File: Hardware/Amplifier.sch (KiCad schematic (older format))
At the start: 1 part, among them U401 PAM8019KGR

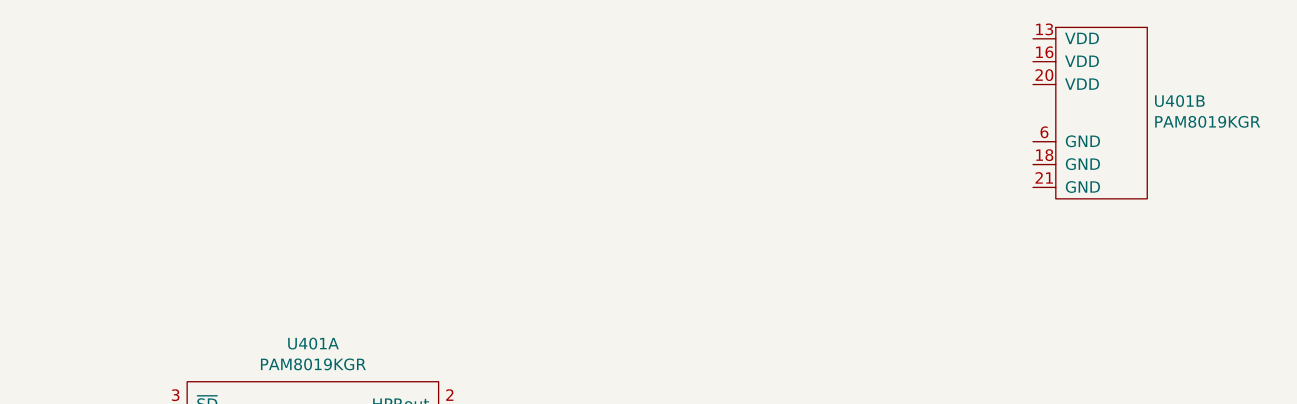
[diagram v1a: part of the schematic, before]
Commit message: Now putting in power and passives.
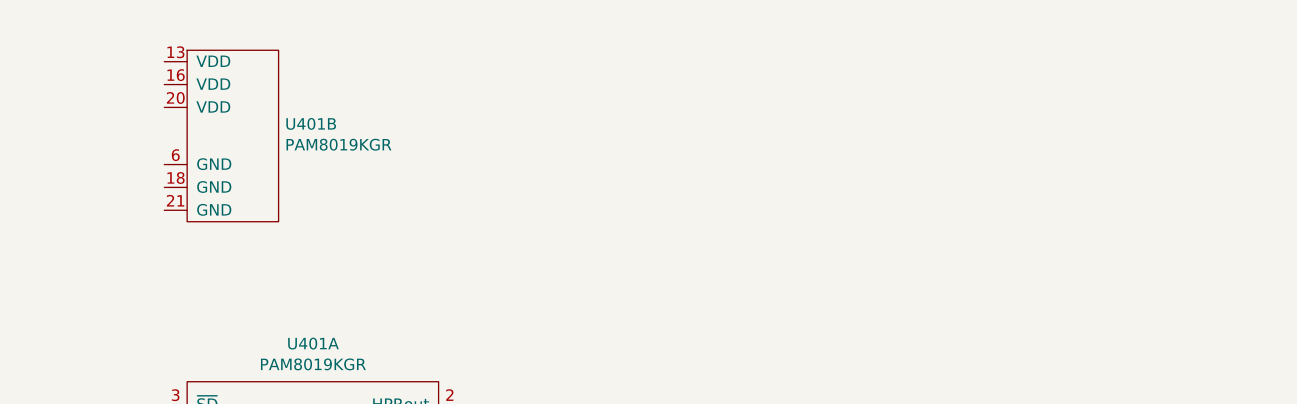
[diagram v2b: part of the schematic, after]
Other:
- moved on the sheet: U401B
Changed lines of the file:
@@
 L OHMC2022:PAM8019KGR U401
 U 2 1 61361640
-P 8850 1800
+P 5050 1900
 AR Path="/611E3218/611E330D/61361640" Ref="U401"  Part="2"
 AR Path="/61375092/611E330D/61361640" Ref="U?"  Part="2"
-F 0 "U401" H 9078 1826 50  0000 L CNN
-F 1 "PAM8019KGR" H 9078 1735 50  0000 L CNN
-F 2 "Package_DFN_QFN:QFN-20-1EP_4x4mm_P0.5mm_EP2.6x2.6mm" H 8550 800 50  0001 C CNN
-F 3 "www.diodes.com/assets/Datasheets/PAM8019.pdf" H 8550 800 50  0001 C CNN
-	2    8850 1800
+F 0 "U401" H 5278 1926 50  0000 L CNN
+F 1 "PAM8019KGR" H 5278 1835 50  0000 L CNN
+F 2 "Package_DFN_QFN:QFN-20-1EP_4x4mm_P0.5mm_EP2.6x2.6mm" H 4750 900 50  0001 C CNN
+F 3 "www.diodes.com/assets/Datasheets/PAM8019.pdf" H 4750 900 50  0001 C CNN
+	2    5050 1900
 	1    0    0    -1
 $EndComp

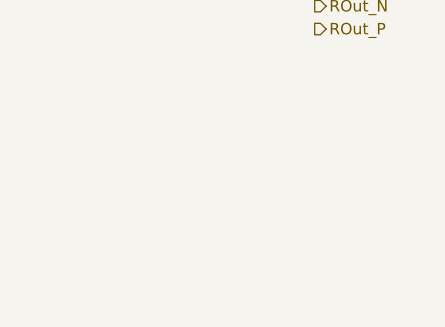
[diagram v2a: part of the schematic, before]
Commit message: Power connectivity going in.
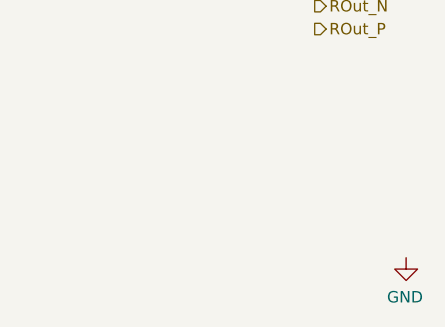
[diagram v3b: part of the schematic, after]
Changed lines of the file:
@@
 Text HLabel 7550 3600 2    50   Output ~ 0
 ROut_P
+$Comp
+L power:GND #PWR?
+U 1 1 613B2112
+P 7950 4600
+F 0 "#PWR?" H 7950 4350 50  0001 C CNN
+F 1 "GND" H 7955 4427 50  0000 C CNN
+F 2 "" H 7950 4600 50  0001 C CNN
+F 3 "" H 7950 4600 50  0001 C CNN
+	1    7950 4600
+	-1   0    0    -1
+$EndComp
 $EndSCHEMATC

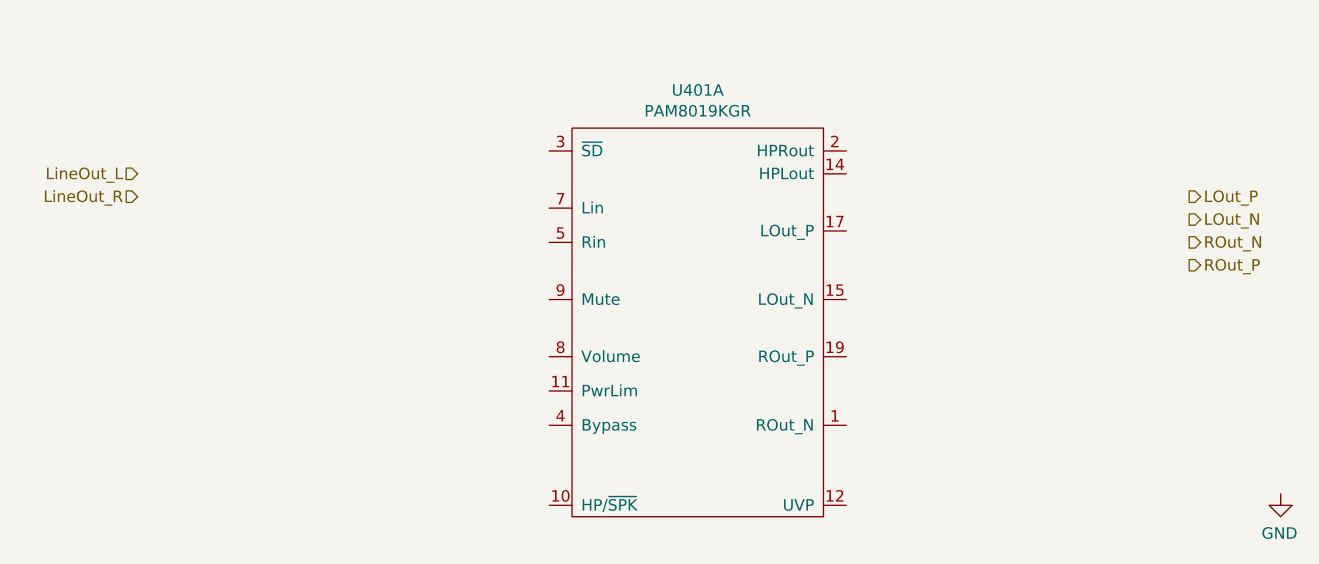
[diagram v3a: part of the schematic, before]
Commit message: Putting in some connectivity. More passives.
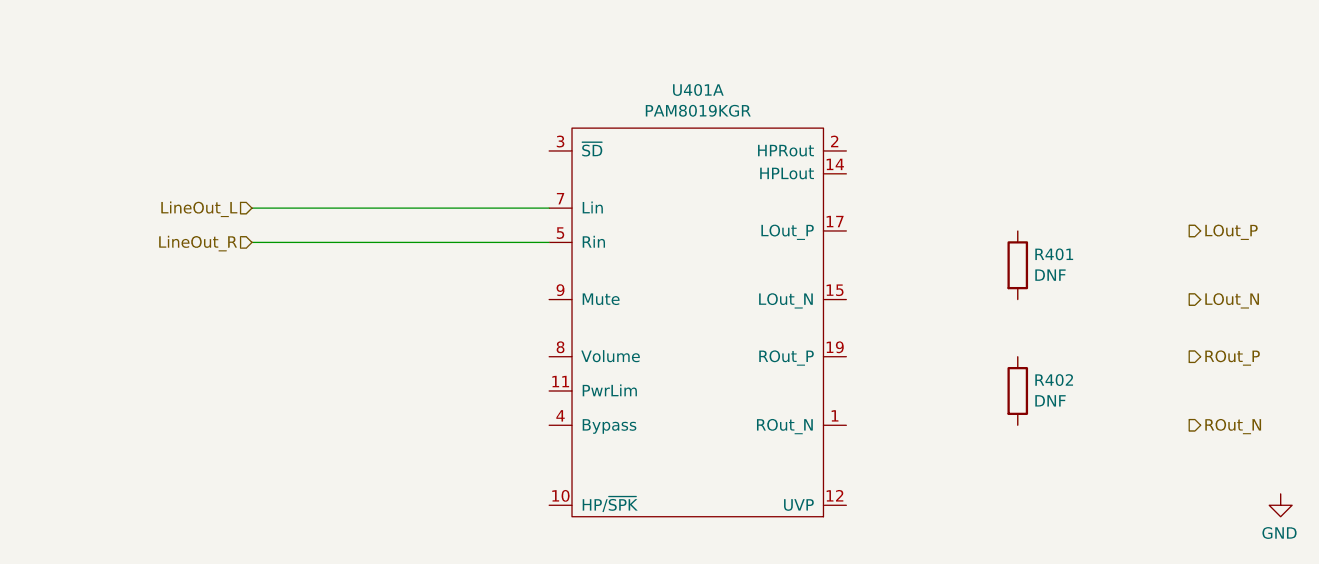
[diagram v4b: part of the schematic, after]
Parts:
- added R401, R402: DNF, Resistor_SMD:R_0603_1608Metric, symbol Device:R
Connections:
- net LineOut_L: now also U401.7 (Lin)
- net LineOut_R: now also U401.5 (Rin)
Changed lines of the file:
@@
 	1    0    0    -1
 $EndComp
-Text HLabel 2950 3300 0    50   Input ~ 0
+Text HLabel 3450 3500 0    50   Input ~ 0
 LineOut_R
-Text HLabel 2950 3200 0    50   Input ~ 0
+Text HLabel 3450 3350 0    50   Input ~ 0
 LineOut_L
-Text HLabel 7550 3300 2    50   Output ~ 0
+Text HLabel 7550 3450 2    50   Output ~ 0
 LOut_P
-Text HLabel 7550 3400 2    50   Output ~ 0
+Text HLabel 7550 3750 2    50   Output ~ 0
 LOut_N
-Text HLabel 7550 3500 2    50   Output ~ 0
+Text HLabel 7550 4300 2    50   Output ~ 0
 ROut_N
-Text HLabel 7550 3600 2    50   Output ~ 0
+Text HLabel 7550 4000 2    50   Output ~ 0
 ROut_P
 $Comp
@@
 U 1 1 613B2112
 P 7950 4600
-F 0 "#PWR?" H 7950 4350 50  0001 C CNN
+AR Path="/611E3335/613B2112" Ref="#PWR?"  Part="1"
+AR Path="/611E3218/611E330D/613B2112" Ref="#PWR0107"  Part="1"
+F 0 "#PWR0107" H 7950 4350 50  0001 C CNN
 F 1 "GND" H 7955 4427 50  0000 C CNN
 F 2 "" H 7950 4600 50  0001 C CNN
@@
 	-1   0    0    -1
 $EndComp
+Wire Wire Line
+	4750 3350 3450 3350
+Wire Wire Line
+	3450 3500 4750 3500
+$Comp
+L Device:R R402
+U 1 1 61464722
+P 6800 4150
+F 0 "R402" H 6870 4196 50  0000 L CNN
+F 1 "DNF" H 6870 4105 50  0000 L CNN
+F 2 "Resistor_SMD:R_0603_1608Metric" V 6730 4150 50  0001 C CNN
+F 3 "~" H 6800 4150 50  0001 C CNN
+	1    6800 4150
+	1    0    0    -1
+$EndComp
+$Comp
+L Device:R R401
+U 1 1 61464F1A
+P 6800 3600
+F 0 "R401" H 6870 3646 50  0000 L CNN
+F 1 "DNF" H 6870 3555 50  0000 L CNN
+F 2 "Resistor_SMD:R_0603_1608Metric" V 6730 3600 50  0001 C CNN
+F 3 "~" H 6800 3600 50  0001 C CNN
+	1    6800 3600
+	1    0    0    -1
+$EndComp
 $EndSCHEMATC

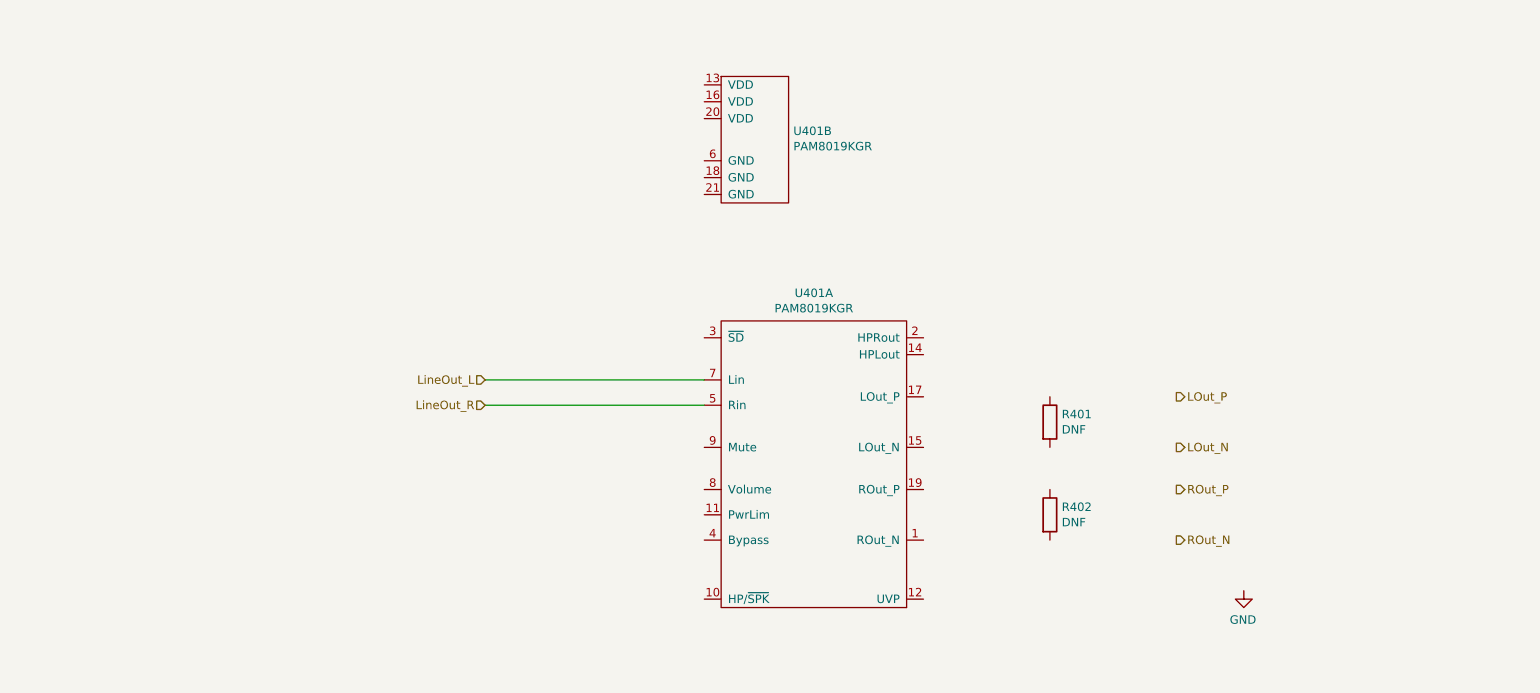
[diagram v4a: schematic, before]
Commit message: Hooking up switches, some more connectivity.
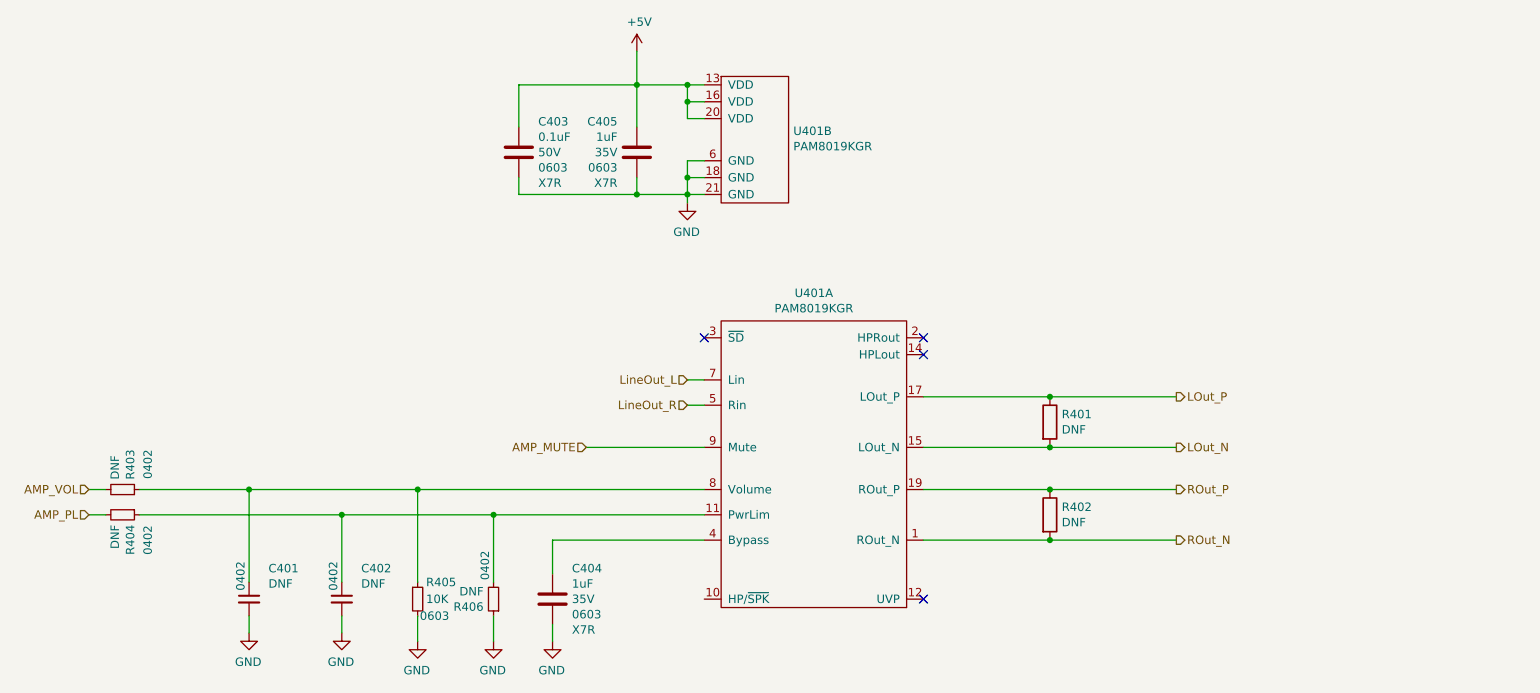
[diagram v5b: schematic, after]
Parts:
- added C401, C402: DNF, Capacitor_SMD:C_0402_1005Metric, symbol Device:C_Small
- added C403: 0.1uF, Capacitor_SMD:C_0603_1608Metric, symbol Device:C
- added C404, C405: 1uF, Capacitor_SMD:C_0603_1608Metric, symbol Device:C
- added R403, R404, R406: DNF, Resistor_SMD:R_0402_1005Metric, symbol Device:R_Small
- added R405: 10K, Resistor_SMD:R_0603_1608Metric, symbol Device:R_Small
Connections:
- net GND: now also U401.18 (GND), U401.21 (GND), U401.6 (GND), C401.2, C402.2, C403.2, C404.2, C405.2, R405.2, R406.1
- net LOut_N: now also R401.2, U401.15 (LOut_N)
- net LOut_P: now also R401.1, U401.17 (LOut_P)
- net ROut_N: now also R402.2, U401.1 (ROut_N)
- net ROut_P: now also R402.1, U401.19 (ROut_P)
- net at U401.11 (PwrLim): now also C402.1, R404.1, R406.2
- net at U401.4 (Bypass): now also C404.1
- net at U401.8 (Volume): now also C401.1, R403.1, R405.1
- net AMP_MUTE: now reaches U401.9 (Mute)
- net +5V: now reaches U401.13 (VDD)
- net +5V: now also U401.16 (VDD), U401.20 (VDD), C403.1, C405.1
- new net AMP_PL: R404.2
- new net AMP_VOL: R403.2
- no-connect marks 0 -> 4

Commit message: Connecting up SAO.
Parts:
- U401: MPN (none) -> PAM8019KGR; MouserPN (none) -> 621-PAM8019KGR
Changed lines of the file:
@@
 $Descr A4 11693 8268
 encoding utf-8
-Sheet 4 9
+Sheet 4 7
 Title ""
 Date ""
@@
 F 2 "Package_DFN_QFN:QFN-20-1EP_4x4mm_P0.5mm_EP2.6x2.6mm" H 5100 2850 50  0001 C CNN
 F 3 "www.diodes.com/assets/Datasheets/PAM8019.pdf" H 5100 2850 50  0001 C CNN
+F 4 "PAM8019KGR" H 5400 3850 50  0001 C CNN "MPN"
+F 5 "621-PAM8019KGR " H 5400 3850 50  0001 C CNN "MouserPN"
 	1    5400 3850
 	1    0    0    -1
